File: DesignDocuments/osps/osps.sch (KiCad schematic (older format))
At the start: 0 parts

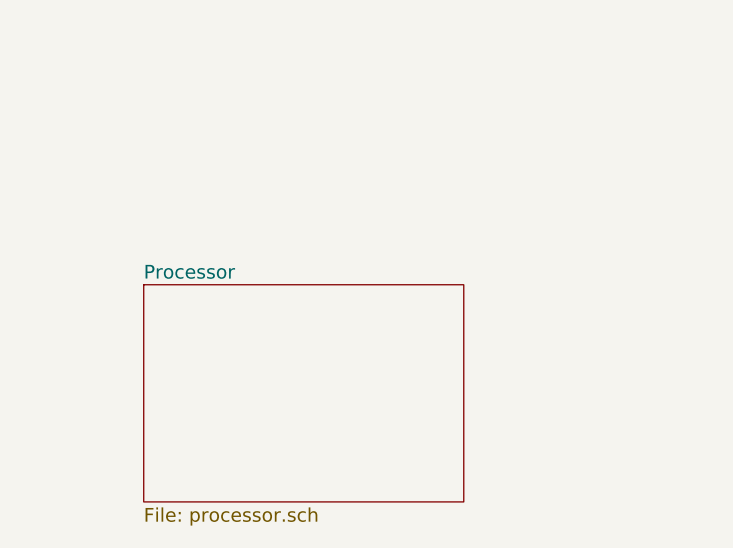
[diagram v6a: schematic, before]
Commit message: added display to mcu pinout with connector
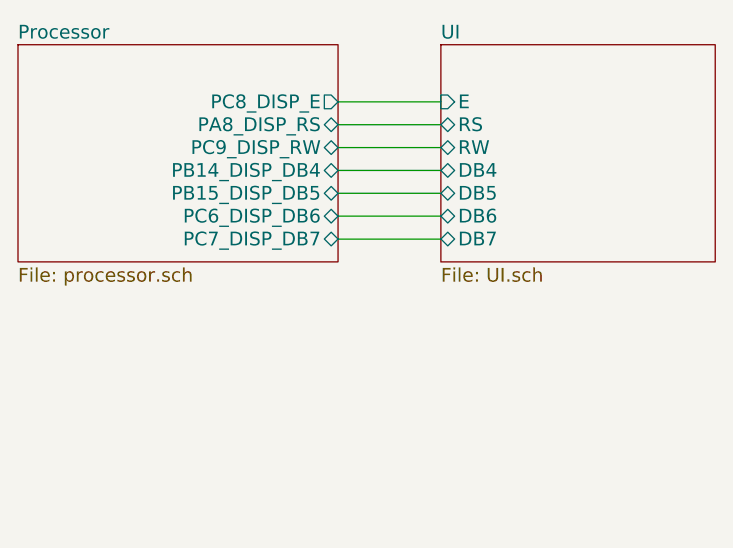
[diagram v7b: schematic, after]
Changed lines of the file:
@@
 LIBS:header-6x1-254
 LIBS:header-10x1-254
+LIBS:header-8x2-254
 LIBS:osps-cache
 EELAYER 25 0
@@
 $Descr A4 11693 8268
 encoding utf-8
-Sheet 1 2
+Sheet 1 3
 Title ""
 Date ""
@@
 $EndDescr
 $Sheet
-S 1700 2100 1400 950
+S 1150 1050 1400 950
 U 5785F670
 F0 "Processor" 60
 F1 "processor.sch" 60
+F2 "PA8_DISP_RS" B R 2550 1400 60
+F3 "PB14_DISP_DB4" B R 2550 1600 60
+F4 "PB15_DISP_DB5" B R 2550 1700 60
+F5 "PC6_DISP_DB6" B R 2550 1800 60
+F6 "PC7_DISP_DB7" B R 2550 1900 60
+F7 "PC8_DISP_E" O R 2550 1300 60
+F8 "PC9_DISP_RW" B R 2550 1500 60
 $EndSheet
+$Sheet
+S 3000 1050 1200 950
+U 578E9575
+F0 "UI" 60
+F1 "UI.sch" 60
+F2 "DB7" B L 3000 1900 60
+F3 "DB5" B L 3000 1700 60
+F4 "E" I L 3000 1300 60
+F5 "RS" B L 3000 1400 60
+F6 "RW" B L 3000 1500 60
+F7 "DB4" B L 3000 1600 60
+F8 "DB6" B L 3000 1800 60
+$EndSheet
+Wire Wire Line
+	3000 1300 2550 1300
+Wire Wire Line
+	2550 1400 3000 1400
+Wire Wire Line
+	3000 1500 2550 1500
+Wire Wire Line
+	2550 1600 3000 1600
+Wire Wire Line
+	3000 1700 2550 1700
+Wire Wire Line
+	2550 1800 3000 1800
+Wire Wire Line
+	3000 1900 2550 1900
 $EndSCHEMATC
